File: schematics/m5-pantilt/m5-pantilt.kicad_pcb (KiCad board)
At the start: 2 copper layers, 50 x 50 mm, 15 parts, among them J1 Conn_02x15_Odd_Even, J2 Conn_02x03_Odd_Even, J3 Conn_02x03_Odd_Even, J4 Conn_02x03_Odd_Even, J5 BAT, J6 Conn_01x04, SW1 SW_SPDT, U1 NL27WZ125

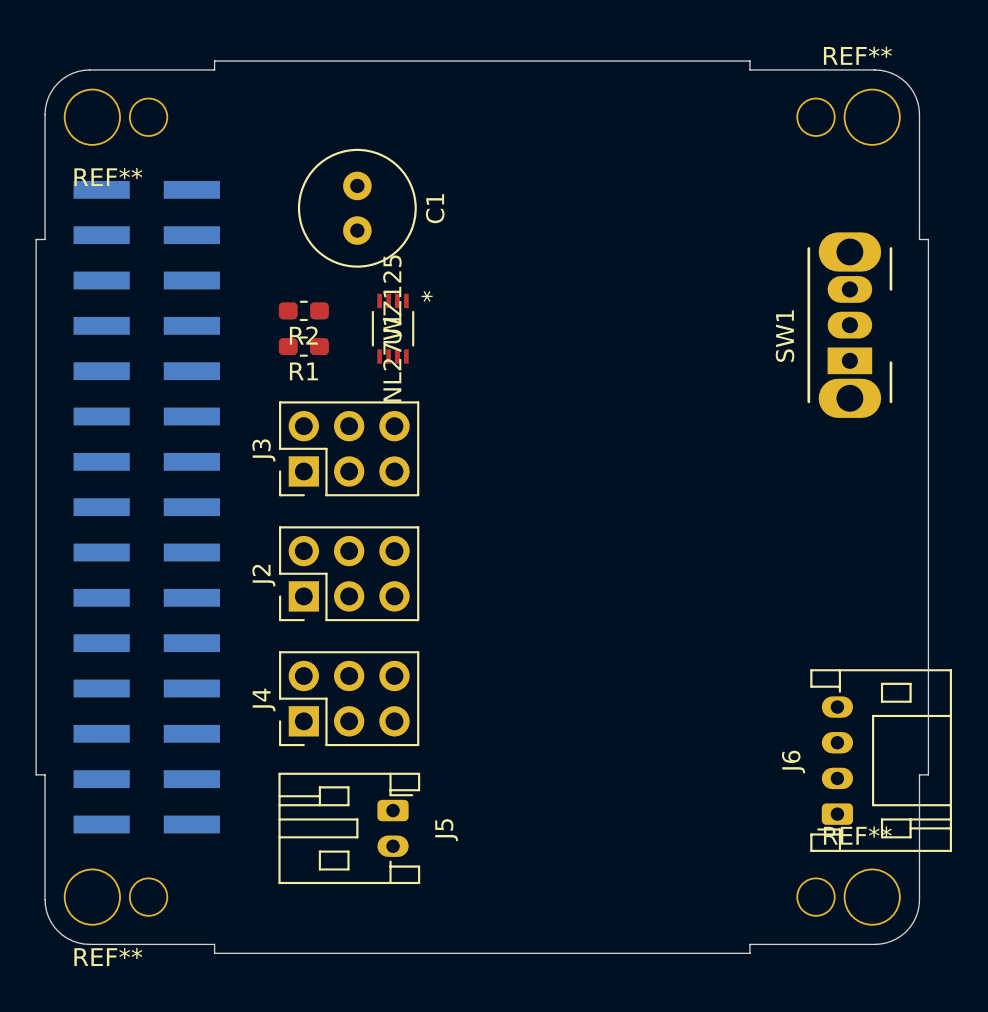
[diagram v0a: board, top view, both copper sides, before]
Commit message: Make schematics and layout
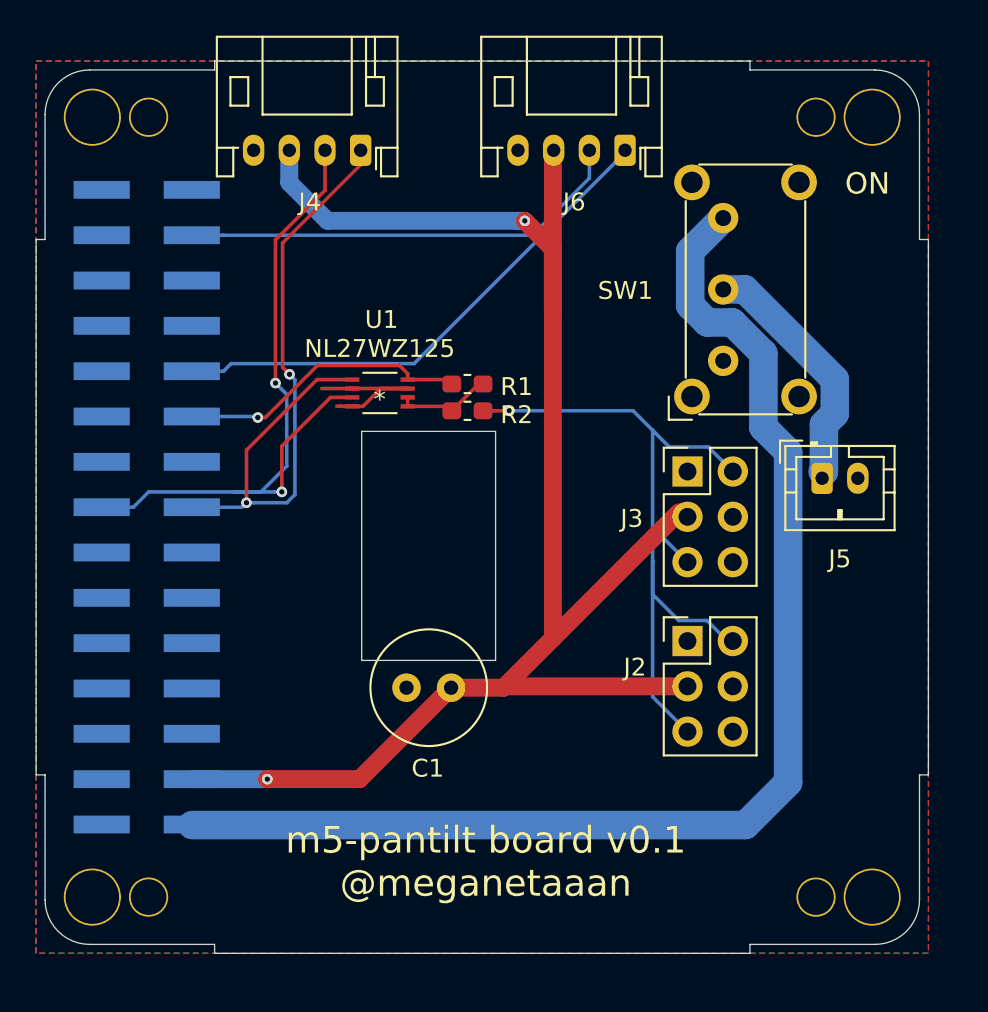
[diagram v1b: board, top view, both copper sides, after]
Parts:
- J4: value Conn_02x03_Odd_Even -> Conn_01x04; footprint Connector_PinHeader_2.54mm:PinHeader_2x03_P2.54mm_Vertical -> Connector_JST:JST_PH_S4B-PH-K_1x04_P2.00mm_Horizontal
- J5: footprint Connector_JST:JST_PH_S2B-PH-K_1x02_P2.00mm_Horizontal -> Connector_JST:JST_PH_B2B-PH-K_1x02_P2.00mm_Vertical
- SW1: footprint Button_Switch_THT:SW_CuK_OS102011MA1QN1_SPDT_Angled -> Button_Switch_THT:SW_E-Switch_EG1224_SPDT_Angled
- moved J6 39.1 mm to (133.0, 55.0), turned to 180 degrees
- moved J4 32.2 mm to (118.2, 55.0), turned to 180 degrees
- moved J5 30.4 mm to (144.0, 73.4), turned to 0 degrees
- moved C1 28.2 mm to (120.8, 85.1), turned to 0 degrees
- moved J2 21.6 mm to (136.5, 82.5), turned to 0 degrees
- moved J3 21.5 mm to (136.5, 73.0), turned to 0 degrees
- moved R2 10.7 mm to (124.2, 69.6)
- moved R1 9.41 mm to (124.2, 68.1), turned to 0 degrees
- moved SW1 7.10 mm to (138.5, 66.8)
- moved U1 3.67 mm to (119.3, 68.6), turned to 0 degrees
- turned J1 to 180 degrees
- renumbered REF** to Hole1, REF** to Hole2, REF** to Hole3, REF** to Hole4
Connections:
- J4 pad 1: GND -> /TXD2
- J4 pad 2: Net-(J2-Pad2) -> /RXD2
- J4 pad 4: Net-(J4-Pad4) -> GND
- SW1 pad 1: Net-(J1-Pad29) -> Net-(SW1-Pad1)
- SW1 pad 3: Net-(SW1-Pad3) -> Net-(J1-Pad29)
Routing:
- net +5V: track 0.00 -> 93.4 mm, vias 0 -> 2
- net Net-(J1-Pad29): track 0.00 -> 69.9 mm
- net Net-(J2-Pad2): track 0.00 -> 43.3 mm, vias 0 -> 1
- net /RXD2: track 0.00 -> 40.8 mm, vias 0 -> 2
- net /TXD2: track 0.00 -> 38.0 mm, vias 0 -> 2
- net /PORTB1: track 0.00 -> 29.5 mm
- net /PORTB2: track 0.00 -> 25.2 mm
- net +3V3: track 0.00 -> 16.4 mm, vias 0 -> 1
- net Net-(J5-Pad1): track 0.00 -> 13.8 mm
- net GND: track 0.00 -> 9.22 mm
- net Net-(R1-Pad2): track 0.00 -> 5.20 mm
- added copper zone on B.Cu, net GND
- added copper zone on F.Cu, net GND
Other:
- outline, holes or cut-outs redrawn
- board text added: "ON"
- board text added: "m5-pantilt board v0.1 @meganetaaan"

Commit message: Add jumper
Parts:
- added JP1: Jumper_3_Bridged12, Jumper:SolderJumper-3_P1.3mm_Bridged12_RoundedPad1.0x1.5mm, B.Cu at (132.3, 84.8)
- added JP2: Jumper_3_Bridged12, Jumper:SolderJumper-3_P1.3mm_Bridged12_RoundedPad1.0x1.5mm, B.Cu at (132.3, 78.4)
- added R3: 1k, Resistor_SMD:R_0603_1608Metric_Pad1.05x0.95mm_HandSolder, F.Cu at (117.0, 82.0)
- added R4: 1k, Resistor_SMD:R_0603_1608Metric_Pad1.05x0.95mm_HandSolder, F.Cu at (115.5, 82.0)
- moved J5 16.2 mm to (140.5, 89.1), turned to 180 degrees
- moved J3 2.65 mm to (137.8, 75.3), turned to 90 degrees
- moved J4 1.81 mm to (120.0, 55.0)
- moved J2 1.33 mm to (137.8, 82.7), turned to 90 degrees
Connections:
- J1 pad 19: Net-(J1-Pad19) -> /PWM1
- J1 pad 20: Net-(J1-Pad20) -> /PWM2
- J3 pad 2: Net-(J2-Pad2) -> Net-(J3-Pad2)
- J3 pad 5: Net-(J2-Pad2) -> Net-(J3-Pad2)
- R2 pad 1: Net-(J2-Pad2) -> Net-(JP2-Pad1)
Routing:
- net Net-(J3-Pad2): track 0.00 -> 25.8 mm, vias 0 -> 1
- net Net-(JP2-Pad3): track 0.00 -> 25.7 mm, vias 0 -> 1
- net Net-(J2-Pad2): track 43.3 -> 19.3 mm, vias 1 -> 2
- net Net-(JP1-Pad3): track 0.00 -> 19.1 mm, vias 0 -> 1
- net Net-(J5-Pad1): track 13.8 -> 32.1 mm
- net Net-(JP2-Pad1): track 0.00 -> 13.6 mm, vias 0 -> 1
- net +5V: track 93.4 -> 106.1 mm, vias 2 -> 1
- net /PWM2: track 0.00 -> 12.6 mm, vias 0 -> 1
- net /PWM1: track 0.00 -> 9.02 mm, vias 0 -> 1
- net /RXD2: track 40.8 -> 35.3 mm
- net /PORTB1: track 29.5 -> 31.1 mm
- net /TXD2: track 38.0 -> 36.9 mm
- net GND: vias 0 -> 77
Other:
- board text added: "PWM"
- board text added: "TTL"

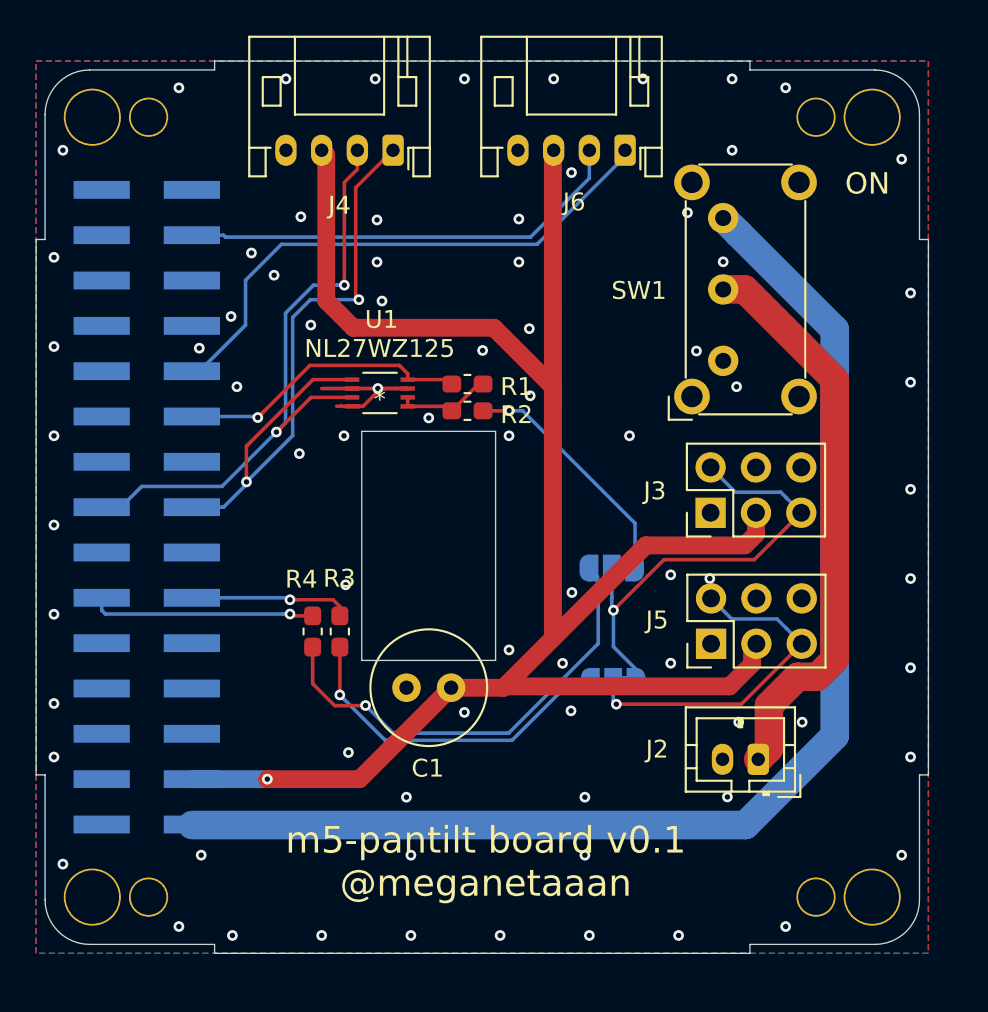
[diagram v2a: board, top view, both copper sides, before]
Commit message: Adjust connectors
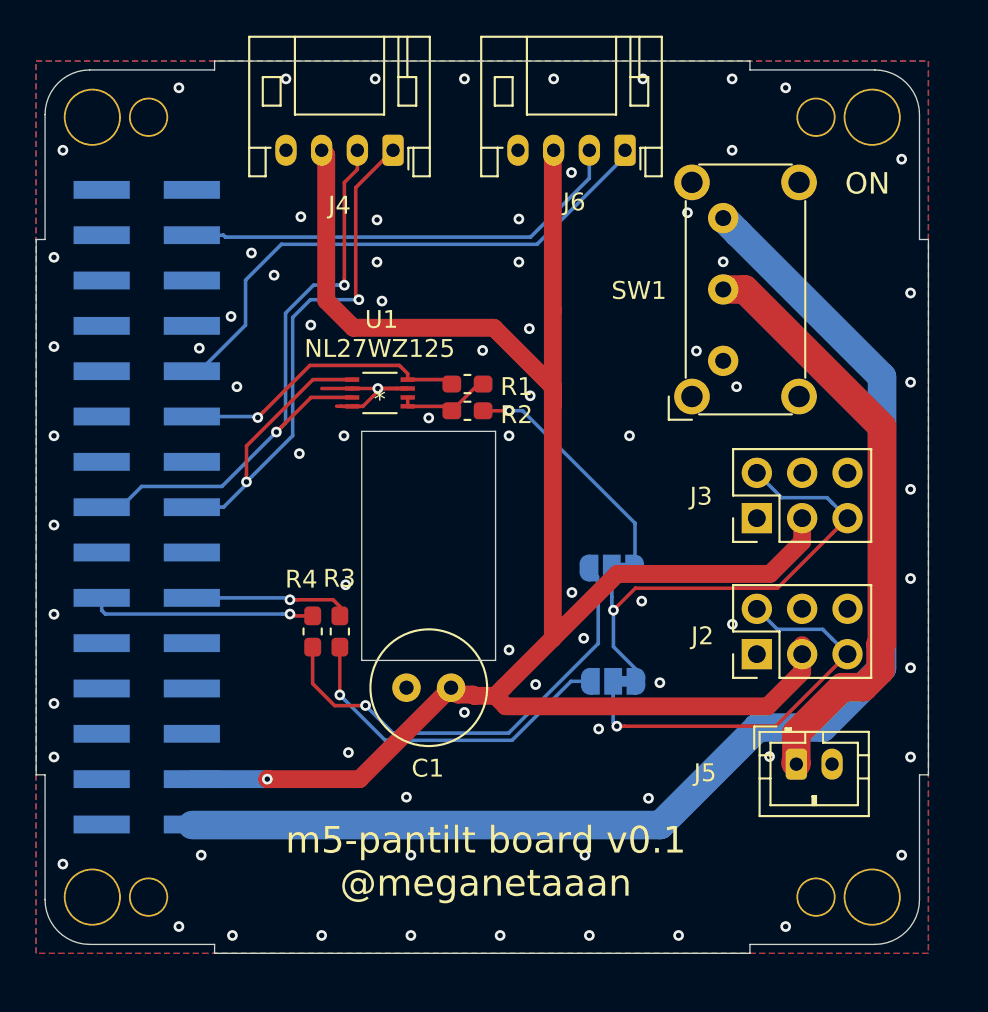
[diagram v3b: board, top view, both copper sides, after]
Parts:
- moved J2 2.63 mm to (140.4, 83.2)
- moved J3 2.61 mm to (140.4, 75.6)
- moved J5 2.15 mm to (142.6, 89.4), turned to 0 degrees
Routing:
- net +5V: track 106.1 -> 112.9 mm
- net Net-(J2-Pad2): track 19.3 -> 23.3 mm, vias 2 -> 1
- net Net-(J3-Pad2): track 25.8 -> 28.2 mm
- net Net-(J5-Pad1): track 32.1 -> 33.7 mm
- net Net-(J1-Pad29): track 69.7 -> 71.3 mm

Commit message: Adjust
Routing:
- net GND: vias 77 -> 78
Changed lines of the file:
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@@
     (thickness 1.6)
     (drawings 32)
-    (tracks 265)
+    (tracks 266)
     (zones 0)
     (modules 19)
@@
   (via (at 126.5 71) (size 0.6) (drill 0.3) (layers F.Cu B.Cu) (net 1))
   (via (at 130.0228 79.7816) (size 0.6) (drill 0.3) (layers F.Cu B.Cu) (net 1))
-  (via (at 133.25 71) (size 0.6) (drill 0.3) (layers F.Cu B.Cu) (net 1))
+  (via (at 130.4292 71.3234) (size 0.6) (drill 0.3) (layers F.Cu B.Cu) (net 1))
   (via (at 141.0972 88.9764) (size 0.6) (drill 0.3) (layers F.Cu B.Cu) (net 1))
   (via (at 124 86.5) (size 0.6) (drill 0.3) (layers F.Cu B.Cu) (net 1))
@@
   (via (at 139.0144 81.5596) (size 0.6) (drill 0.3) (layers F.Cu B.Cu) (net 1))
   (via (at 134.3154 91.3132) (size 0.6) (drill 0.3) (layers F.Cu B.Cu) (net 1))
+  (via (at 145.6692 71.2726) (size 0.6) (drill 0.3) (layers F.Cu B.Cu) (net 1))
   (segment (start 108.725 90.24) (end 112.954 90.24) (width 1) (layer B.Cu) (net 2))
   (segment (start 112.954 90.24) (end 112.954 90.24) (width 1) (layer B.Cu) (net 2))
@@
   (segment (start 140.4368 87.3508) (end 144.069 87.3508) (width 1.6) (layer B.Cu) (net 25))
   (segment (start 144.069 87.3508) (end 147.4 84.0198) (width 1.6) (layer B.Cu) (net 25))
-  (segment (start 144.616001 82.386001) (end 145.466 83.236) (width 0.2) (layer B.Cu) (net 27) (status 1000000))
-  (segment (start 141.536001 81.846001) (end 144.076001 81.846001) (width 0.2) (layer B.Cu) (net 27) (status 1000000))
-  (segment (start 140.386 80.696) (end 141.536001 81.846001) (width 0.2) (layer B.Cu) (net 27) (status 1000000))
-  (segment (start 144.076001 81.846001) (end 144.616001 82.386001) (width 0.2) (layer B.Cu) (net 27) (status 1000000))
+  (segment (start 144.616001 82.386001) (end 145.466 83.236) (width 0.2) (layer B.Cu) (net 27))
+  (segment (start 141.536001 81.846001) (end 144.076001 81.846001) (width 0.2) (layer B.Cu) (net 27))
+  (segment (start 140.386 80.696) (end 141.536001 81.846001) (width 0.2) (layer B.Cu) (net 27))
+  (segment (start 144.076001 81.846001) (end 144.616001 82.386001) (width 0.2) (layer B.Cu) (net 27))
   (via (at 132.5374 87.274598) (size 0.6) (drill 0.3) (layers F.Cu B.Cu) (net 27))
   (segment (start 132.3342 84.76) (end 132.3342 87.071398) (width 0.2) (layer B.Cu) (net 27))

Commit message: Refactor
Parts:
- added LOGO: LOGO, m5-pantilt:avatar_small, B.Cu at (125.7, 74.5)
- moved U1 8.16 mm to (118.5, 76.7)
- moved R4 8.01 mm to (123.4, 80.6), turned to 180 degrees
- moved R2 7.93 mm to (123.4, 77.5)
- moved R1 7.76 mm to (123.4, 75.8)
- moved R3 6.98 mm to (123.4, 79.1), turned to 180 degrees
- moved C1 5.69 mm to (126.4, 84.5), turned to 270 degrees
- moved JP1 3.67 mm to (135.3, 82.6)
- moved JP2 3.18 mm to (135.3, 79.3)
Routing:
- net Net-(JP2-Pad3): track 25.7 -> 11.0 mm
- net /PWM2: track 12.6 -> 19.8 mm
- net Net-(JP1-Pad3): track 19.1 -> 12.3 mm
- net /PWM1: track 9.02 -> 14.2 mm
- net Net-(J3-Pad2): track 28.2 -> 24.6 mm
- net /TXD2: track 36.9 -> 33.4 mm
- net +3V3: track 16.4 -> 19.0 mm
- net /RXD2: track 35.3 -> 37.8 mm
- net GND: track 9.22 -> 11.2 mm, vias 78 -> 96
- net Net-(J5-Pad1): track 33.7 -> 35.4 mm
- net +5V: track 112.9 -> 113.8 mm, vias 1 -> 0
- net Net-(J2-Pad2): track 23.3 -> 22.5 mm
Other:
- outline, holes or cut-outs redrawn

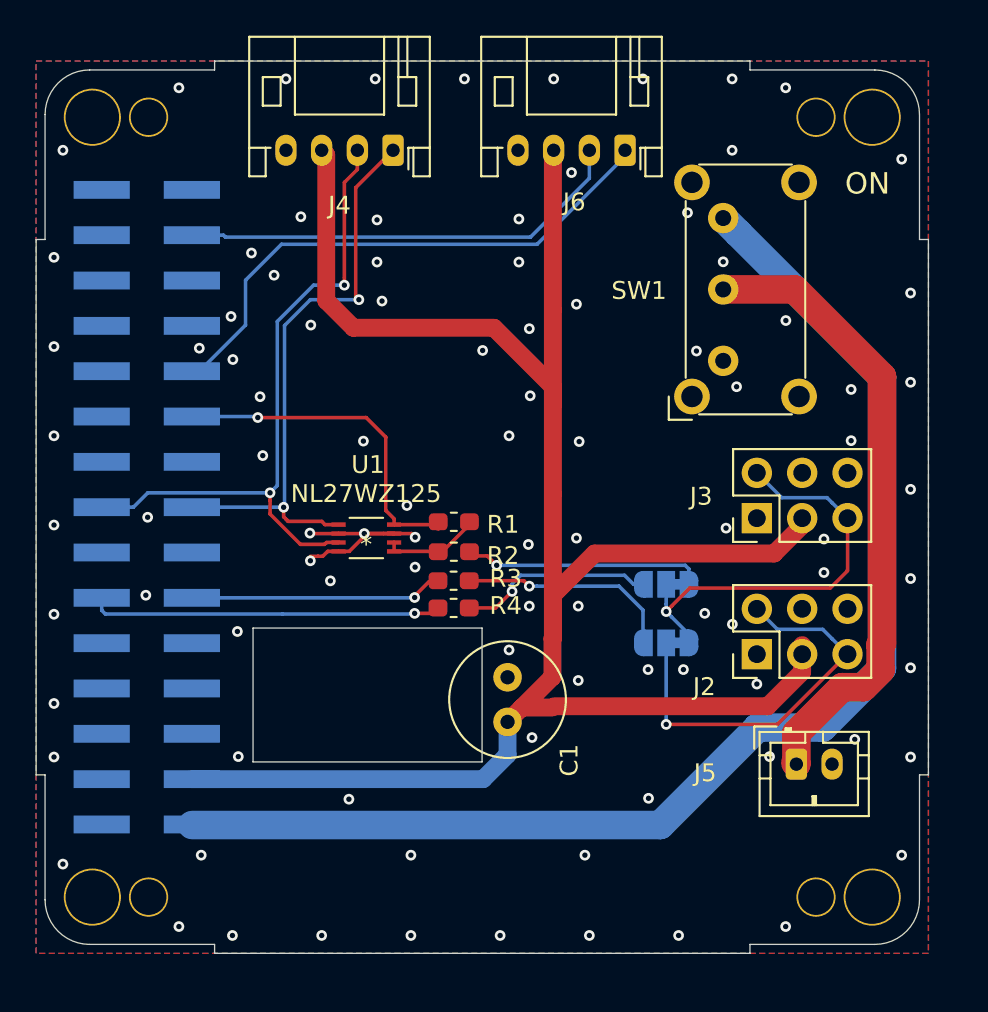
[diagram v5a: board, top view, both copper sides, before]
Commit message: Update schematics
* Core2 available
* Add diode for power stability
* Add 5V-GND connector
* Separete Jumper
* Open Jumper
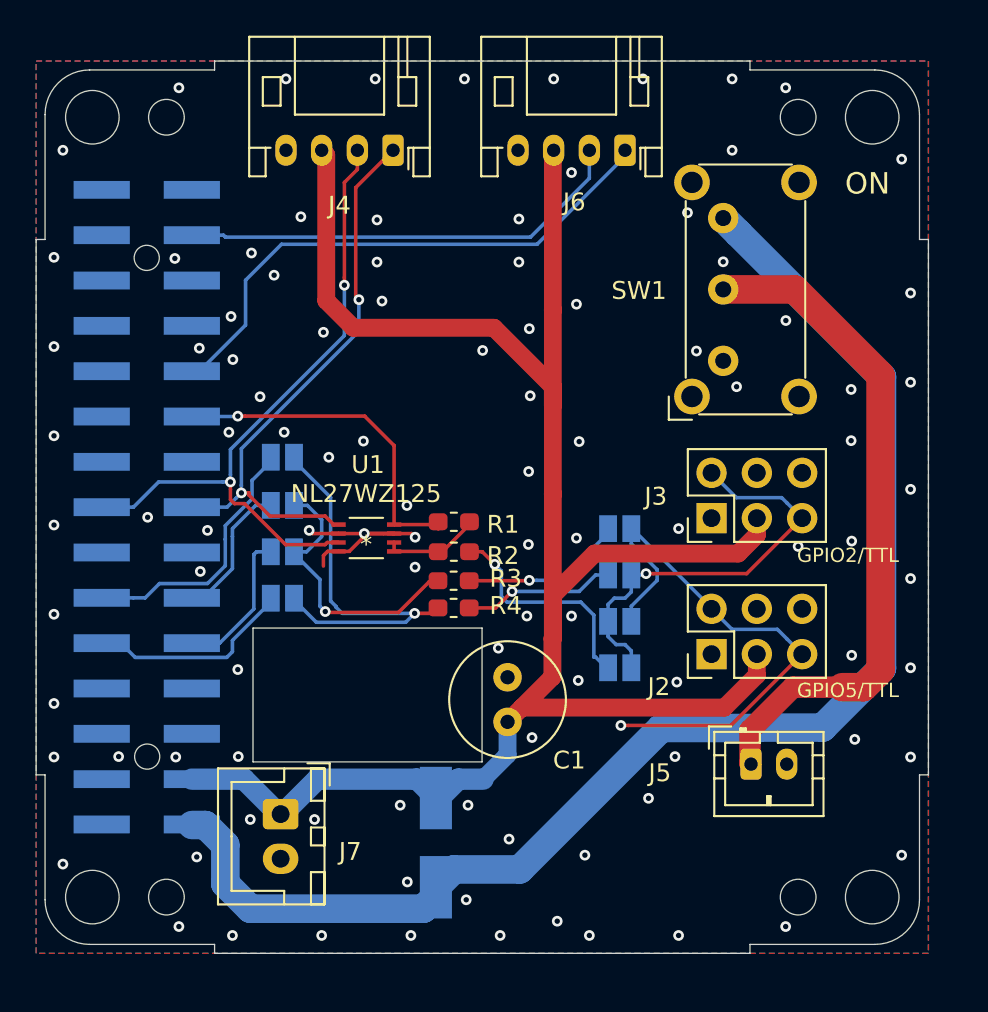
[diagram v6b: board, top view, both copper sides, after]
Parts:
- added D1: D, Diode_SMD:D_SMA_Handsoldering, B.Cu at (122.4, 93.8)
- added J7: 5V_POWER, Connector_JST:JST_XH_B2B-XH-A_1x02_P2.50mm_Vertical, F.Cu at (113.7, 92.2)
- added JP3: Jumper_2_Open, Jumper:SolderJumper-2_P1.3mm_Open_Pad1.0x1.5mm, B.Cu at (132.7, 81.4)
- added JP4: Jumper_2_Open, Jumper:SolderJumper-2_P1.3mm_Open_Pad1.0x1.5mm, B.Cu at (132.7, 84.0)
- added JP5: Jumper_2_Open, Jumper:SolderJumper-2_P1.3mm_Open_Pad1.0x1.5mm, B.Cu at (113.8, 74.9)
- added JP6: Jumper_2_Open, Jumper:SolderJumper-2_P1.3mm_Open_Pad1.0x1.5mm, B.Cu at (113.8, 77.5)
- added JP7: Jumper_2_Open, Jumper:SolderJumper-2_P1.3mm_Open_Pad1.0x1.5mm, B.Cu at (113.8, 72.2)
- added JP8: Jumper_2_Open, Jumper:SolderJumper-2_P1.3mm_Open_Pad1.0x1.5mm, B.Cu at (113.8, 80.1)
- JP1, JP2: value Jumper_3_Bridged12 -> Jumper_2_Open; footprint Jumper:SolderJumper-3_P1.3mm_Bridged12_RoundedPad1.0x1.5mm -> Jumper:SolderJumper-2_P1.3mm_Open_Pad1.0x1.5mm
- moved JP1 6.91 mm to (132.7, 76.2), turned to 0 degrees
- moved JP2 2.66 mm to (132.7, 78.8), turned to 0 degrees
- moved J2 2.54 mm to (137.8, 83.2)
- moved J3 2.54 mm to (137.8, 75.6)
- moved J5 2.54 mm to (140.1, 89.4)
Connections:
- J1 pad 19: /PWM1 -> /PWM1_C1
- J1 pad 20: /PWM2 -> /PWM2_C1
- J1 pad 21: Net-(J1-Pad21) -> /PWM1_C2
- J1 pad 22: Net-(J1-Pad22) -> /PWM2_C2
- JP1 pad 1: Net-(J3-Pad2) -> Net-(JP1-Pad1)
- R2 pad 1: Net-(JP2-Pad1) -> Net-(JP4-Pad2)
- R3 pad 1: Net-(JP1-Pad3) -> Net-(JP1-Pad1)
- R4 pad 1: Net-(JP2-Pad3) -> Net-(JP2-Pad1)
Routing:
- net /PWM2_C1: track 0.00 -> 14.7 mm
- net Net-(JP4-Pad2): track 0.00 -> 12.7 mm, vias 0 -> 1
- net Net-(JP1-Pad3): track 12.3 -> 0.00 mm, vias 1 -> 0
- net /PWM2_C2: track 0.00 -> 11.6 mm
- net Net-(JP2-Pad3): track 11.0 -> 0.00 mm, vias 1 -> 0
- net Net-(JP1-Pad1): track 0.00 -> 9.14 mm, vias 0 -> 1
- net Net-(J2-Pad2): track 22.5 -> 30.7 mm
- net /PWM1_C2: track 0.00 -> 8.23 mm
- net /PWM1_C1: track 0.00 -> 7.79 mm
- net Net-(D1-Pad2): track 71.3 -> 76.7 mm
- net Net-(JP2-Pad1): track 13.4 -> 8.55 mm
- net /PWM2: track 19.8 -> 22.9 mm
- net Net-(J5-Pad1): track 35.4 -> 38.0 mm
- net +5V: track 113.8 -> 111.5 mm
- net /PWM1: track 14.2 -> 15.9 mm
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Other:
- outline, holes or cut-outs redrawn
- board text added: "Anode"
- board text added: "Cathode"
- board text added: "Core1"
- board text added: "Core2"
- board text added: "GPIO2/TTL"
- board text added: "GPIO5/TTL"
- board text added: "Rx"
- board text added: "Tx"
- board text added: "m5-pantilt board v0.1.1 @meganetaaan"
- board text removed: "m5-pantilt board v0.1 @meganetaaan"
